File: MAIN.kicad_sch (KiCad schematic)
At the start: 0 parts

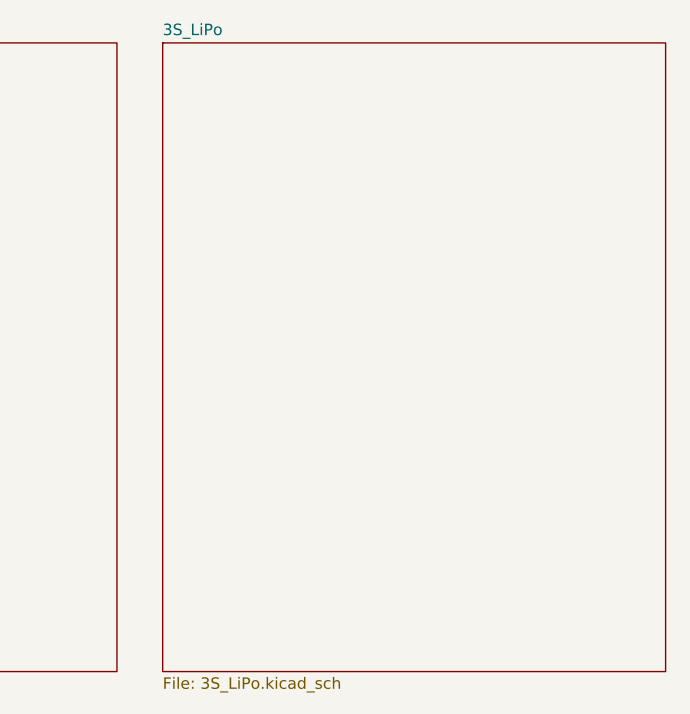
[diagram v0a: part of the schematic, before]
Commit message: Add files via upload
Updated BQ76952 schematic with passive cell balancing, voltage readout to ESP32 and temperature sensing. To do: Connect remaining pins on BQ76952 to ESP32.
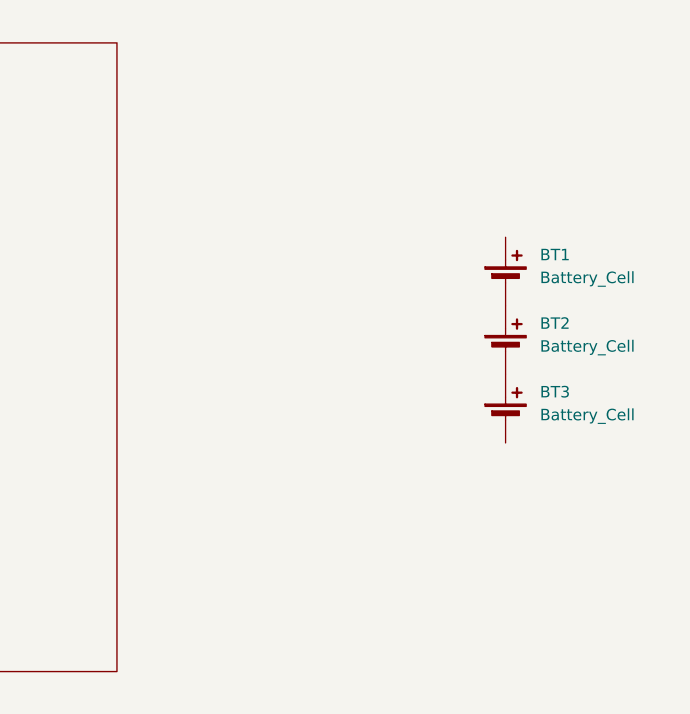
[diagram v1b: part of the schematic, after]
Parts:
- added BT1, BT2, BT3: Battery_Cell, symbol Device:Battery_Cell
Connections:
- new net: BT2.2 (-), BT3.1 (+)
- new net: BT1.2 (-), BT2.1 (+)
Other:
- removed sheet 3S_LiPo

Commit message: REV1 PCB that was sent to production (PCBWAY)
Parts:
- removed BT1, BT2, BT3: Battery_Cell, symbol Device:Battery_Cell
- added J6: Conn_01x04_Socket, Connector_JST:JST_XH_B4B-XH-A_1x04_P2.50mm_Vertical, symbol Connector:Conn_01x04_Socket
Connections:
- new net +BATT: J6.1 (Pin_1)
- new net 1P: J6.3 (Pin_3)
- new net 2P: J6.2 (Pin_2)
- new net VSS: J6.4 (Pin_4)
